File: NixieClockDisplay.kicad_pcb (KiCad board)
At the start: 2 copper layers, 160 x 70 mm, 75 parts, among them J2 CONN_01X03, J3 CONN_01X02, J4 Conn_02x02_Odd_Even, J5 Conn_01x04, SW1 RotaryEncoder_Switch_RGB, U1 TPIC6B595, U2 TPIC6B595, U3 TPIC6B595, U4 TPIC6B595, U5 TPIC6B595, U6 TPIC6B595, U7 WE-FDSM_DC/DC_5V, U8 AdafruitProTrinket5V, U9 WS2811

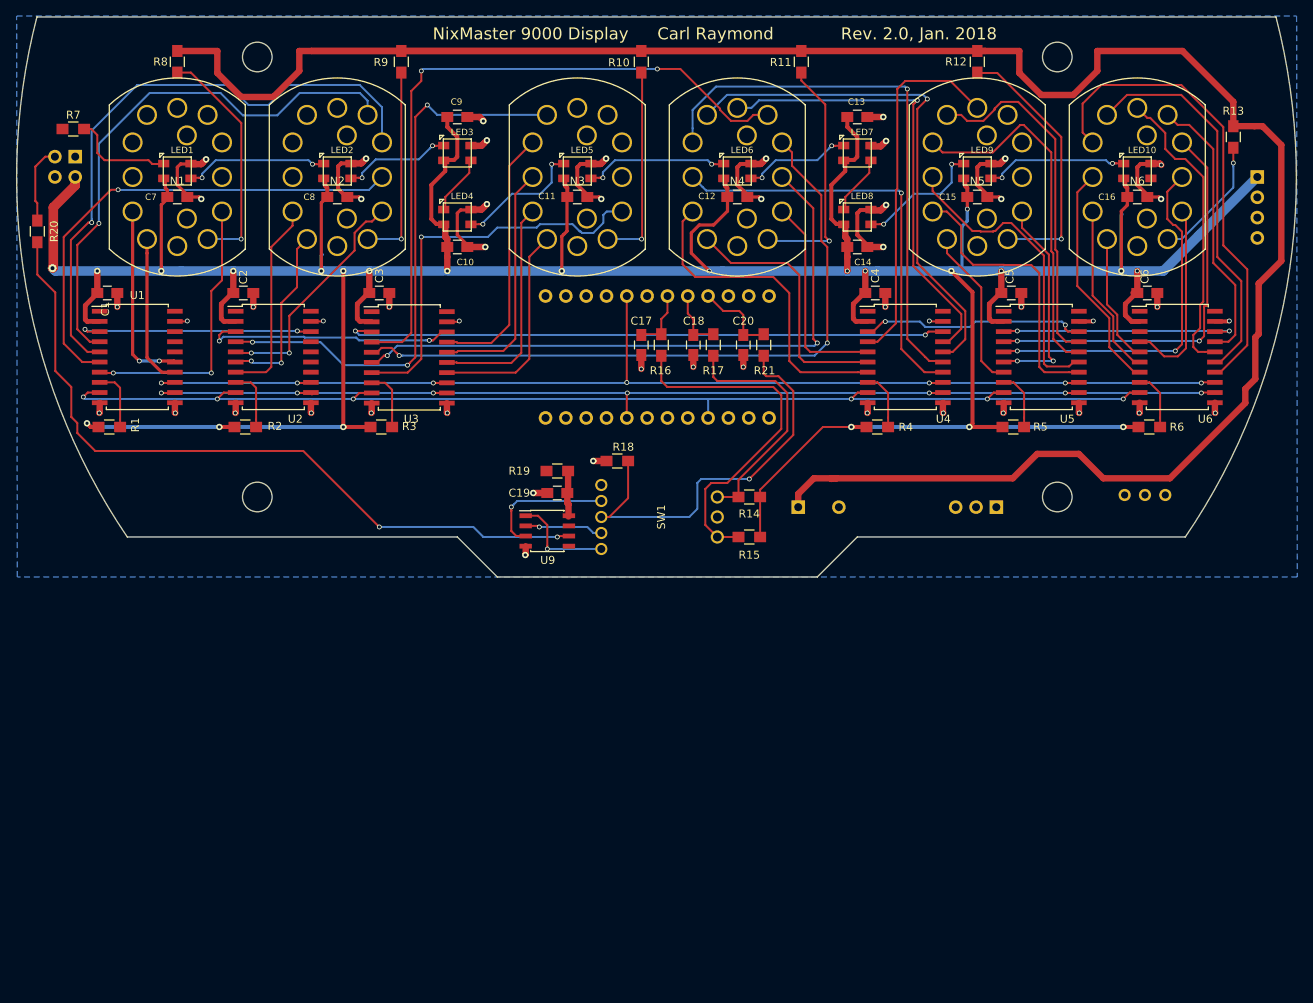
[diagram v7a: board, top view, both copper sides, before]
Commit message: Add Adafruit OLED display
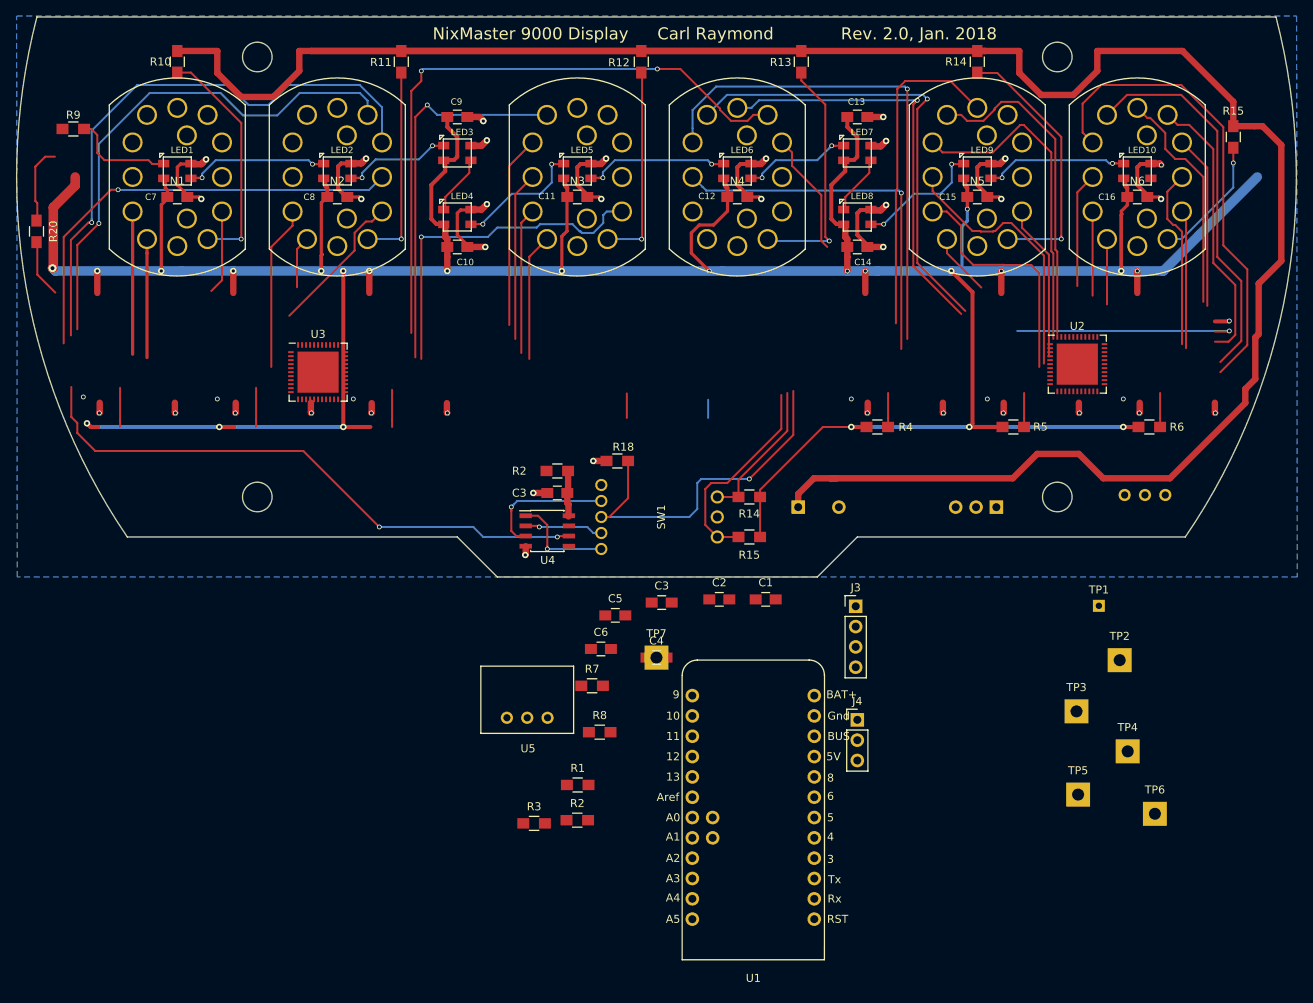
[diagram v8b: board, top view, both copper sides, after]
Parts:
- removed C17, C18, C20: .01uF, Capacitors_SMD:C_0805_HandSoldering
- removed J5: Conn_01x04, Pin_Headers:Pin_Header_Straight_1x04_Pitch2.54mm
- removed R16, R17, R21: 10K, Resistors_SMD:R_0805_HandSoldering
- removed the U4 at (181.0, 82.5)
- removed U6: TPIC6B595, Housings_SOIC:SOIC-20W_7.5x12.8mm_Pitch1.27mm
- removed U8: AdafruitProTrinket5V, NixieClockDisplay:Adafruit_Trinket_Pro
- added J3: Conn_01x04, Pin_Headers:Pin_Header_Straight_1x04_Pitch2.54mm, F.Cu at (174.8, 113.7)
- added R7: 10K, Resistors_SMD:R_0805_HandSoldering, F.Cu at (141.8, 123.6)
- added R8: 22K, Resistors_SMD:R_0805_HandSoldering, F.Cu at (142.8, 129.4)
- added TP1: TEST_1P, Measurement_Points:Measurement_Point_Square-TH_Small, F.Cu at (205.2, 113.6)
- added TP2: TEST_1P, Measurement_Points:Measurement_Point_Square-TH_Big, F.Cu at (207.8, 120.4)
- added TP3: TEST_1P, Measurement_Points:Measurement_Point_Square-TH_Big, F.Cu at (202.4, 126.8)
- added TP4: TEST_1P, Measurement_Points:Measurement_Point_Square-TH_Big, F.Cu at (208.8, 131.8)
- added TP5: TEST_1P, Measurement_Points:Measurement_Point_Square-TH_Big, F.Cu at (202.6, 137.2)
- added TP6: TEST_1P, Measurement_Points:Measurement_Point_Square-TH_Big, F.Cu at (212.2, 139.6)
- added TP7: TEST_1P, Measurement_Points:Measurement_Point_Square-TH_Big, F.Cu at (149.9, 120.1)
- J4: value Conn_02x02_Odd_Even -> Conn_01x03; footprint Pin_Headers:Pin_Header_Straight_2x02_Pitch2.54mm -> Pin_Headers:Pin_Header_Straight_1x03_Pitch2.54mm; moved to F.Cu
- R1: value 10K -> 33R
- R14, R15, R4, R6: value 10K -> 22K
- R2: value 10K -> 100
- U1: value TPIC6B595 -> AdafruitProTrinket5V; footprint Housings_SOIC:SOIC-20W_7.5x12.8mm_Pitch1.27mm -> NixieClockDisplay:Adafruit_Trinket_Pro
- U2, U3: value TPIC6B595 -> HV5523; footprint Housings_SOIC:SOIC-20W_7.5x12.8mm_Pitch1.27mm -> Housings_DFN_QFN:QFN-44-1EP_7x7mm_Pitch0.5mm
- U5: value TPIC6B595 -> WE-FDSM_DC/DC_5V; footprint Housings_SOIC:SOIC-20W_7.5x12.8mm_Pitch1.27mm -> NixieClockDisplay:WPMDL9500xx
- moved J4 120.5 mm to (175.0, 127.9), turned to 0 degrees
- moved U2 100.5 mm to (202.5, 83.4)
- moved U1 95.4 mm to (162.0, 138.8)
- moved C1 90.8 mm to (163.6, 112.8), turned to 0 degrees
- moved C6 81.5 mm to (142.9, 119.0), turned to 0 degrees
- moved U5 77.2 mm to (133.7, 125.3)
- moved R1 73.7 mm to (140.1, 136.0), turned to 0 degrees
- moved C2 70.8 mm to (157.8, 112.8), turned to 0 degrees
- moved R2 64.3 mm to (140.0, 140.4), turned to 0 degrees
- moved C5 63.8 mm to (144.8, 114.8), turned to 0 degrees
- moved C4 53.2 mm to (149.9, 120.1), turned to 0 degrees
- moved R3 53.1 mm to (134.6, 140.8), turned to 0 degrees
- moved C3 52.4 mm to (150.6, 113.2), turned to 0 degrees
- moved U3 11.5 mm to (107.6, 84.4)
- moved R20 0.10 mm to (72.4, 66.8)
- renumbered C19 to C3, J3 to J1, R8 to R10, R9 to R11, R10 to R12, R11 to R13, R12 to R14, R13 to R15, R19 to R2, R7 to R9, U9 to U4
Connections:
- C1 pad 1: GND -> +5V
- C1 pad 2: +5V -> GND
- C2 pad 1: GND -> +5V
- C2 pad 2: +5V -> GND
- C3 pad 1: Net-(C19-Pad1) -> Net-(C3-Pad1)
- C3 pad 1: GND -> Net-(C3-Pad1)
- C3 pad 2: +5V -> GND
- C4 pad 1: GND -> ROTARY_PB
- C4 pad 2: +5V -> GND
- C5 pad 1: GND -> ROTARY_A
- C5 pad 2: +5V -> GND
- C6 pad 1: GND -> ROTARY_B
- C6 pad 2: +5V -> GND
- J1 pad 1: Net-(J3-Pad1) -> +180V
- J2 pad 2: /SHDN -> SHDN
- J4 pad 1: Net-(J4-Pad1) -> +5V
- J4 pad 2: Net-(J4-Pad2) -> GND
- J4 pad 3: +5V -> Net-(J4-Pad3)
- LED10 pad 1: Net-(LED10-Pad1) -> Net-(J4-Pad3)
- N1 pad 10: /HOUR_20 -> HOUR_20
- N1 pad 11: /HOUR_10 -> HOUR_10
- N1 pad 2: /HOUR_00 -> HOUR_00
- N1 pad 3: Net-(N1-Pad3) -> HOUR_90
- N1 pad 4: Net-(N1-Pad4) -> HOUR_80
- N1 pad 5: Net-(N1-Pad5) -> HOUR_70
- N1 pad 6: Net-(N1-Pad6) -> HOUR_60
- N1 pad 7: Net-(N1-Pad7) -> HOUR_50
- N1 pad 8: /HOUR_40 -> HOUR_40
- N1 pad 9: /HOUR_30 -> HOUR_30
- N2 pad 10: /HOUR_2 -> HOUR_2
- N2 pad 11: /HOUR_1 -> HOUR_1
- N2 pad 2: /HOUR_0 -> HOUR_0
- N2 pad 3: /HOUR_9 -> HOUR_9
- N2 pad 4: /HOUR_8 -> HOUR_8
- N2 pad 5: /HOUR_7 -> HOUR_7
- N2 pad 6: /HOUR_6 -> HOUR_6
- N2 pad 7: /HOUR_5 -> HOUR_5
- N2 pad 8: /HOUR_4 -> HOUR_4
- N2 pad 9: /HOUR_3 -> HOUR_3
- N3 pad 10: /MIN_20 -> MIN_20
- N3 pad 11: /MIN_10 -> MIN_10
- N3 pad 2: /MIN_00 -> MIN_00
- N3 pad 3: Net-(N3-Pad3) -> MIN_90
- N3 pad 4: Net-(N3-Pad4) -> MIN_80
- N3 pad 5: Net-(N3-Pad5) -> MIN_70
- N3 pad 6: Net-(N3-Pad6) -> MIN_60
- N3 pad 7: /MIN_50 -> MIN_50
- N3 pad 8: /MIN_40 -> MIN_40
- N3 pad 9: /MIN_30 -> MIN_30
- N4 pad 10: /MIN_2 -> MIN_2
- N4 pad 11: /MIN_1 -> MIN_1
- N4 pad 2: /MIN_0 -> MIN_0
- N4 pad 3: /MIN_9 -> MIN_9
- N4 pad 4: /MIN_8 -> MIN_8
- N4 pad 5: /MIN_7 -> MIN_7
- N4 pad 6: /MIN_6 -> MIN_6
- N4 pad 7: /MIN_5 -> MIN_5
- N4 pad 8: /MIN_4 -> MIN_4
- N4 pad 9: /MIN_3 -> MIN_3
- N5 pad 10: /SEC_20 -> SEC_20
- N5 pad 11: /SEC_10 -> SEC_10
- N5 pad 2: /SEC_00 -> SEC_00
- N5 pad 3: Net-(N5-Pad3) -> SEC_90
- N5 pad 4: Net-(N5-Pad4) -> SEC_80
- N5 pad 5: Net-(N5-Pad5) -> SEC_70
- N5 pad 6: /SEC_60 -> SEC_60
- N5 pad 7: /SEC_50 -> SEC_50
- N5 pad 8: /SEC_40 -> SEC_40
- N5 pad 9: /SEC_30 -> SEC_30
- N6 pad 10: /SEC_2 -> SEC_2
- N6 pad 11: /SEC_1 -> SEC_1
- N6 pad 2: /SEC_0 -> SEC_0
- N6 pad 3: /SEC_9 -> SEC_9
- N6 pad 4: /SEC_8 -> SEC_8
- N6 pad 5: /SEC_7 -> SEC_7
- N6 pad 6: /SEC_6 -> SEC_6
- N6 pad 7: /SEC_5 -> SEC_5
- N6 pad 8: /SEC_4 -> SEC_4
- N6 pad 9: /SEC_3 -> SEC_3
- R1 pad 1: Net-(R1-Pad1) -> PIXEL_DATA
- R1 pad 2: +5V -> Net-(R1-Pad2)
- R10 pad 2: Net-(J3-Pad1) -> +180V
- R11 pad 2: Net-(J3-Pad1) -> +180V
- R12 pad 2: Net-(J3-Pad1) -> +180V
- R13 pad 2: Net-(J3-Pad1) -> +180V
- R14 pad 2: Net-(J3-Pad1) -> +180V
- R14 pad 1: +5V -> Net-(N5-Pad1)
- R14 pad 2: Net-(R14-Pad2) -> +180V
- R15 pad 2: Net-(J3-Pad1) -> +180V
- R15 pad 1: +5V -> Net-(N6-Pad1)
- R15 pad 2: Net-(R15-Pad2) -> +180V
- R2 pad 1: Net-(C19-Pad1) -> Net-(C3-Pad1)
- R2 pad 1: Net-(R2-Pad1) -> Net-(C3-Pad1)
- R3 pad 1: Net-(R3-Pad1) -> GND
- R3 pad 2: +5V -> Net-(R3-Pad2)
- R4 pad 1: Net-(R4-Pad1) -> ROTARY_PB
- R4 pad 2: +5V -> Net-(R3-Pad2)
- R5 pad 1: Net-(R5-Pad1) -> +5V
- R5 pad 2: +5V -> Net-(R5-Pad2)
- R6 pad 1: Net-(R6-Pad1) -> ROTARY_A
- R6 pad 2: +5V -> Net-(R5-Pad2)
- SW1 pad 3: Net-(R18-Pad2) -> Net-(R3-Pad2)
- SW1 pad A: Net-(R15-Pad2) -> Net-(R5-Pad2)
- SW1 pad B: Net-(R14-Pad2) -> Net-(R7-Pad2)
- U1 pad 1: (no net) -> /NIXIE_LE
- U1 pad 10: GND -> Net-(U1-Pad10)
- U1 pad 11: GND -> Net-(U1-Pad11)
- U1 pad 12: /RCK -> Net-(U1-Pad12)
- U1 pad 13: /SRCK -> Net-(U1-Pad13)
- U1 pad 14: /HOUR_10 -> Net-(U1-Pad14)
- U1 pad 15: /HOUR_20 -> Net-(U1-Pad15)
- U1 pad 16: /HOUR_30 -> SHDN
- U1 pad 17: /HOUR_40 -> NIXIE_BLANK
- U1 pad 18: Net-(U1-Pad18) -> 60HZ_OUT
- U1 pad 19: GND -> PIXEL_DATA
- U1 pad 2: +5V -> Net-(U1-Pad2)
- U1 pad 20: (no net) -> TIME_IN
- U1 pad 3: Net-(U1-Pad3) -> NIXIE_DATA
- U1 pad 4: /HOUR_7 -> Net-(U1-Pad4)
- U1 pad 5: /HOUR_8 -> NIXIE_CLK
- U1 pad 6: /HOUR_9 -> Net-(U1-Pad6)
- U1 pad 7: /HOUR_00 -> ROTARY_A
- U1 pad 8: Net-(R1-Pad1) -> ROTARY_B
- U1 pad 9: //G -> ROTARY_PB
- U2 pad 1: (no net) -> SEC_00
- U2 pad 10: GND -> SEC_90
- U2 pad 11: GND -> MIN_0
- U2 pad 12: /RCK -> MIN_1
- U2 pad 13: /SRCK -> MIN_2
- U2 pad 14: /HOUR_3 -> MIN_3
- U2 pad 15: /HOUR_4 -> MIN_4
- U2 pad 16: /HOUR_5 -> MIN_5
- U2 pad 17: /HOUR_6 -> MIN_6
- U2 pad 18: Net-(U1-Pad3) -> MIN_7
- U2 pad 19: GND -> MIN_8
- U2 pad 2: +5V -> SEC_10
- U2 pad 20: (no net) -> MIN_9
- U2 pad 3: Net-(U2-Pad3) -> SEC_20
- U2 pad 4: /MIN_50 -> SEC_30
- U2 pad 5: /HOUR_0 -> SEC_40
- U2 pad 6: /HOUR_1 -> SEC_50
- U2 pad 7: /HOUR_2 -> SEC_60
- U2 pad 8: Net-(R2-Pad1) -> SEC_70
- U2 pad 9: //G -> SEC_80
- U3 pad 1: (no net) -> HOUR_0
- U3 pad 10: GND -> HOUR_9
- U3 pad 11: GND -> HOUR_00
- U3 pad 12: /RCK -> HOUR_10
- U3 pad 13: /SRCK -> HOUR_20
- U3 pad 14: /MIN_10 -> HOUR_30
- U3 pad 15: /MIN_20 -> HOUR_40
- U3 pad 16: /MIN_30 -> HOUR_50
- U3 pad 17: /MIN_40 -> HOUR_60
- U3 pad 18: Net-(U2-Pad3) -> HOUR_70
- U3 pad 19: GND -> HOUR_80
- U3 pad 2: +5V -> HOUR_1
- U3 pad 20: (no net) -> HOUR_90
- U3 pad 3: Net-(U3-Pad3) -> HOUR_2
- U3 pad 4: /MIN_7 -> HOUR_3
- U3 pad 5: /MIN_8 -> HOUR_4
- U3 pad 6: /MIN_9 -> HOUR_5
- U3 pad 7: /MIN_00 -> HOUR_6
- U3 pad 8: Net-(R3-Pad1) -> HOUR_7
- U3 pad 9: //G -> HOUR_8
- U4 pad 6: Net-(R20-Pad2) -> Net-(R1-Pad2)
- U4 pad 8: Net-(C19-Pad1) -> Net-(C3-Pad1)
- U5 pad 1: (no net) -> +12V
- U5 pad 2: +5V -> GND
- U5 pad 3: Net-(U5-Pad3) -> +5V
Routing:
- net +180V: track 0.00 -> 338.5 mm
- net Net-(J3-Pad1): track 322.0 -> 0.00 mm
- net /SRCK: track 151.3 -> 0.00 mm, vias 7 -> 0
- net //G: track 147.2 -> 0.00 mm, vias 6 -> 0
- net /RCK: track 143.6 -> 0.00 mm, vias 7 -> 0
- net /MIN_8: track 85.6 -> 0.00 mm, vias 2 -> 0
- net Net-(R20-Pad2): track 92.8 -> 7.23 mm, vias 2 -> 0
- net /MIN_7: track 85.2 -> 0.00 mm, vias 2 -> 0
- net MIN_7: track 0.00 -> 79.7 mm, vias 0 -> 2
- net /MIN_9: track 79.3 -> 0.00 mm, vias 2 -> 0
- net /HOUR_8: track 77.6 -> 0.00 mm, vias 1 -> 0
- net Net-(U3-Pad3): track 75.9 -> 0.00 mm, vias 2 -> 0
- net HOUR_8: track 0.00 -> 73.2 mm, vias 0 -> 1
- net Net-(R1-Pad2): track 0.00 -> 72.9 mm, vias 0 -> 2
- net /MIN_50: track 71.7 -> 0.00 mm, vias 3 -> 0
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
